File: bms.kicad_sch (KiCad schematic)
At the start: 15 parts, among them Q2 TK11S10N1L,LQ, U1 L99BM114-TR

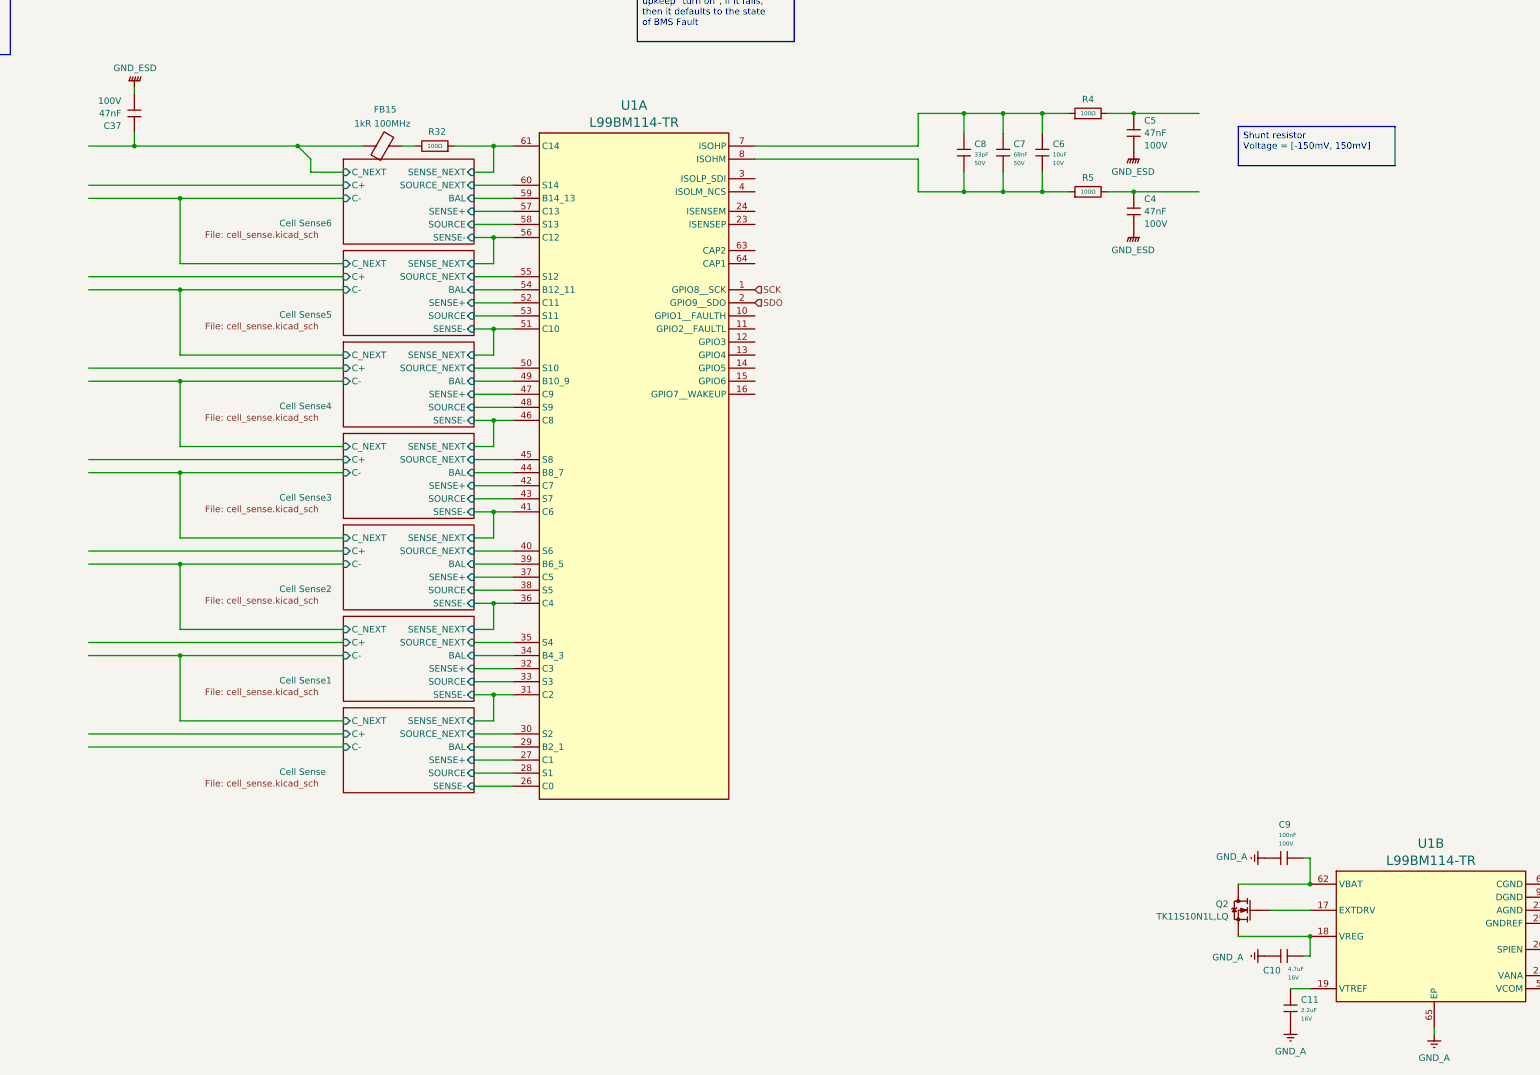
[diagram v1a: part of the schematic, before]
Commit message: updated to use generics for passives
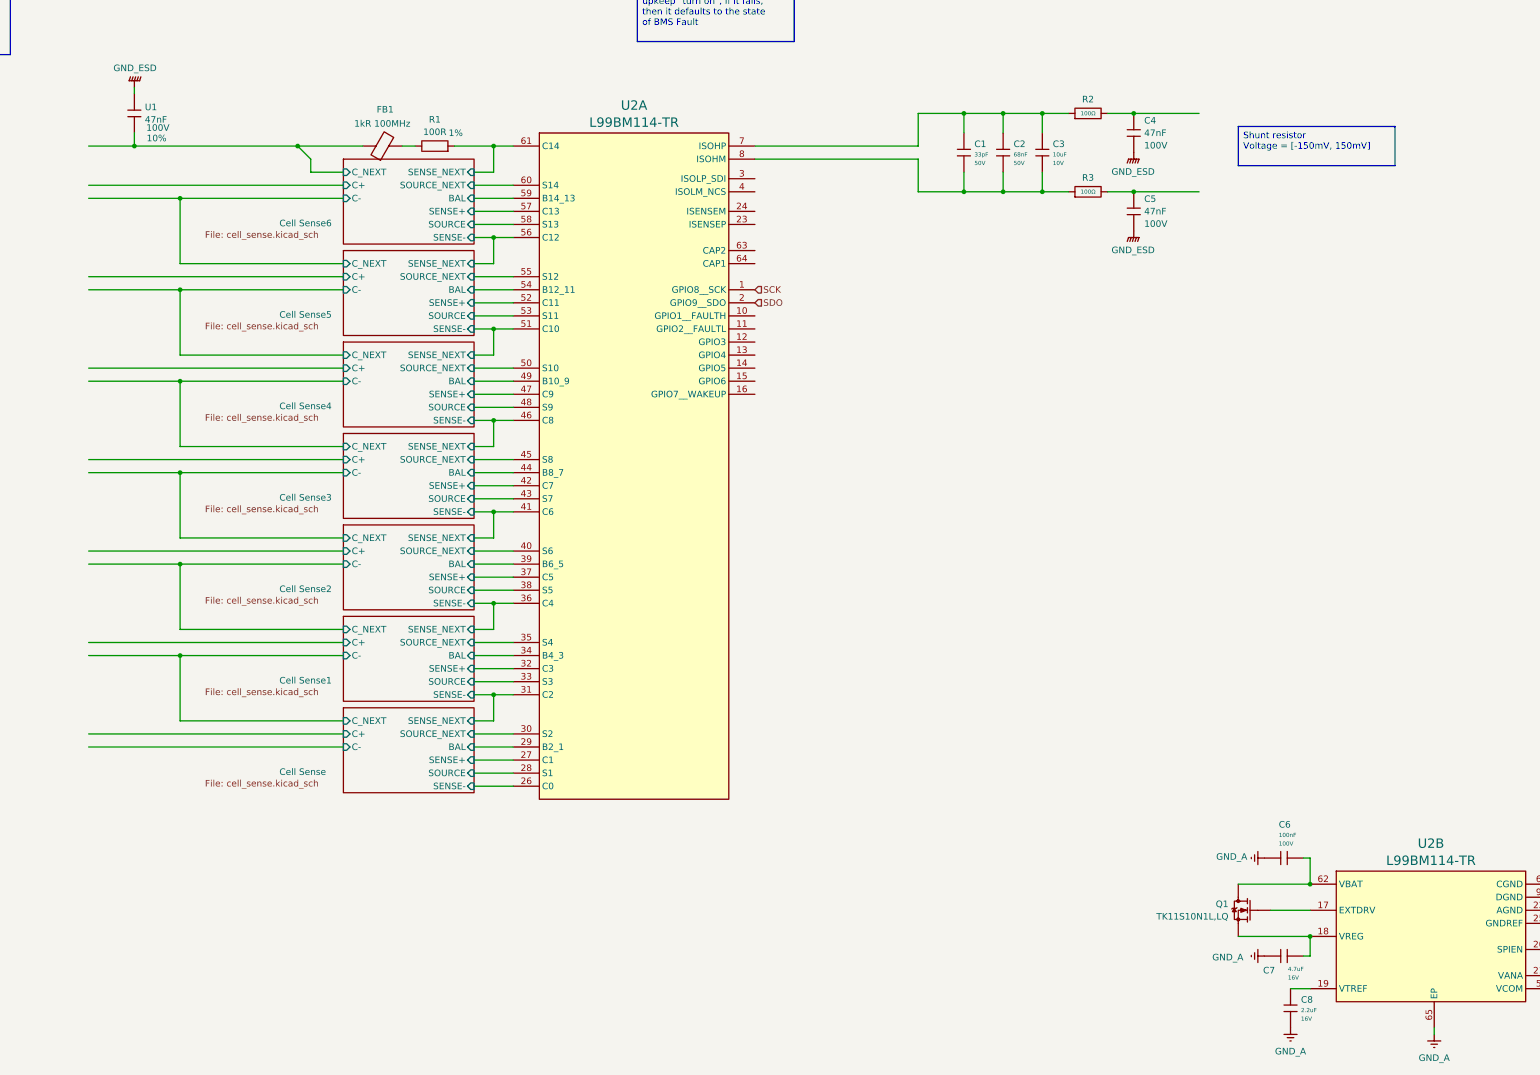
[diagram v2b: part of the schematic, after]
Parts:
- removed C37: 47nF, symbol ct_lib:CC0603KRX7R0BB473
- removed R32: 100Ω, PCM_JLCPCB:R_0402, symbol PCM_JLCPCB-Resistors:0402,100Ω
- added R1: 100R, symbol ct_lib:R
- added U1: 47nF, symbol ct_lib:C
- renumbered C8 to C1, C7 to C2, C6 to C3, C5 to C4, C4 to C5, C9 to C6, C10 to C7, C11 to C8, FB15 to FB1, Q2 to Q1, R4 to R2, R5 to R3, U1 to U2
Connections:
- net Cell Sense6/SENSE_NEXT: now also R1.2
- net GND_ESD: now also U1.1
- net at FB1.1: now also U1.2
- net at FB1.2: now also R1.1

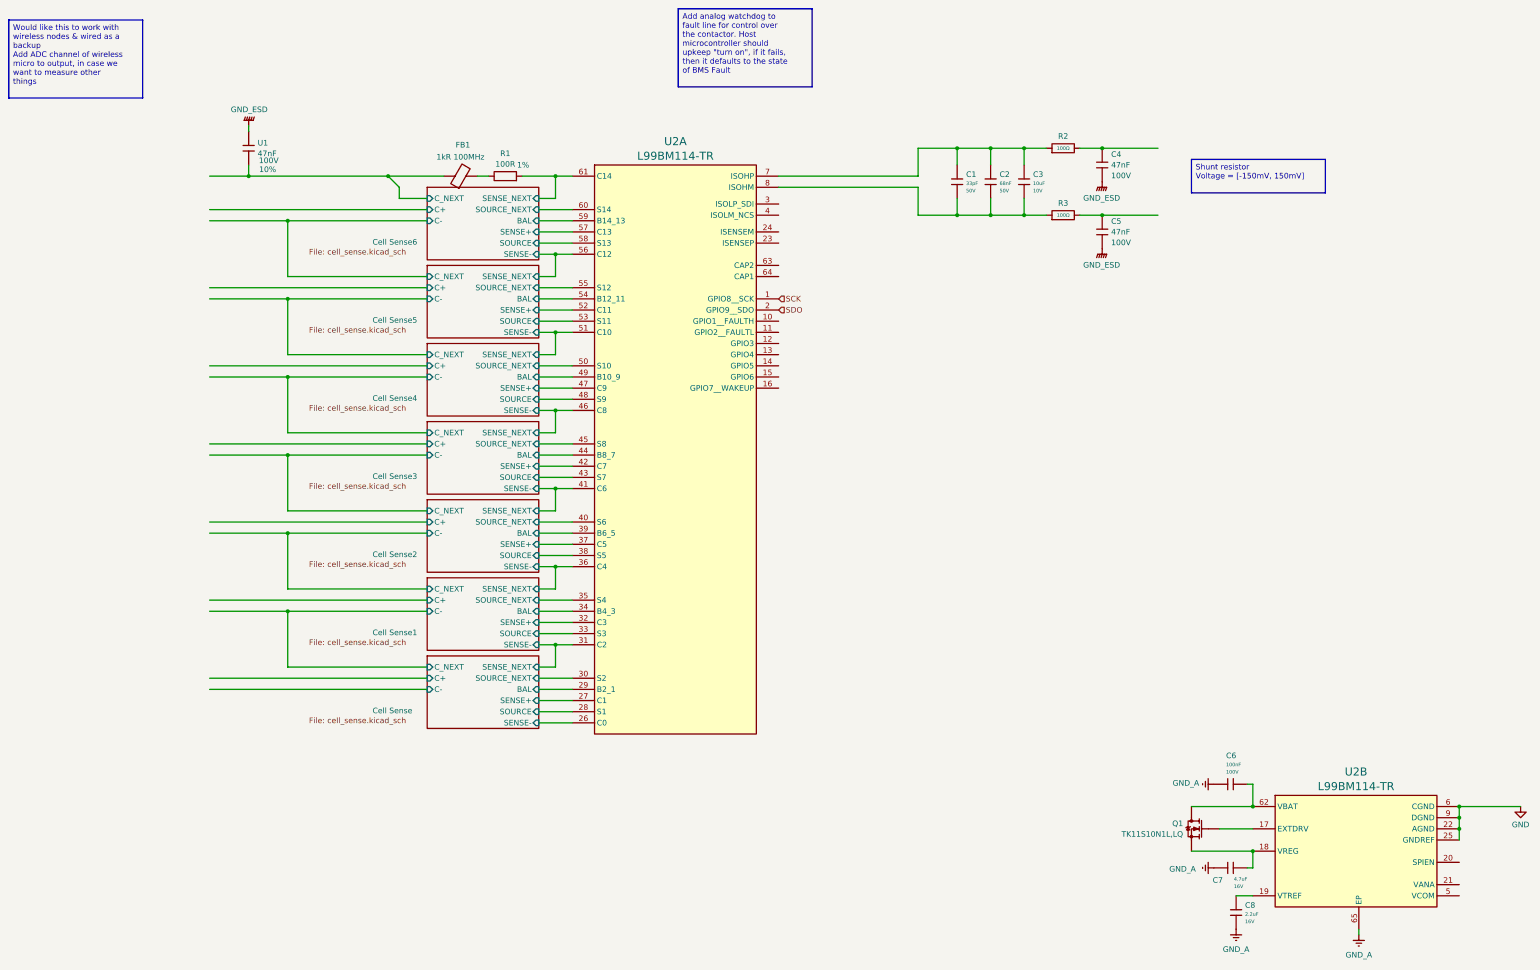
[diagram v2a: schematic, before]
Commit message: added BQ chip
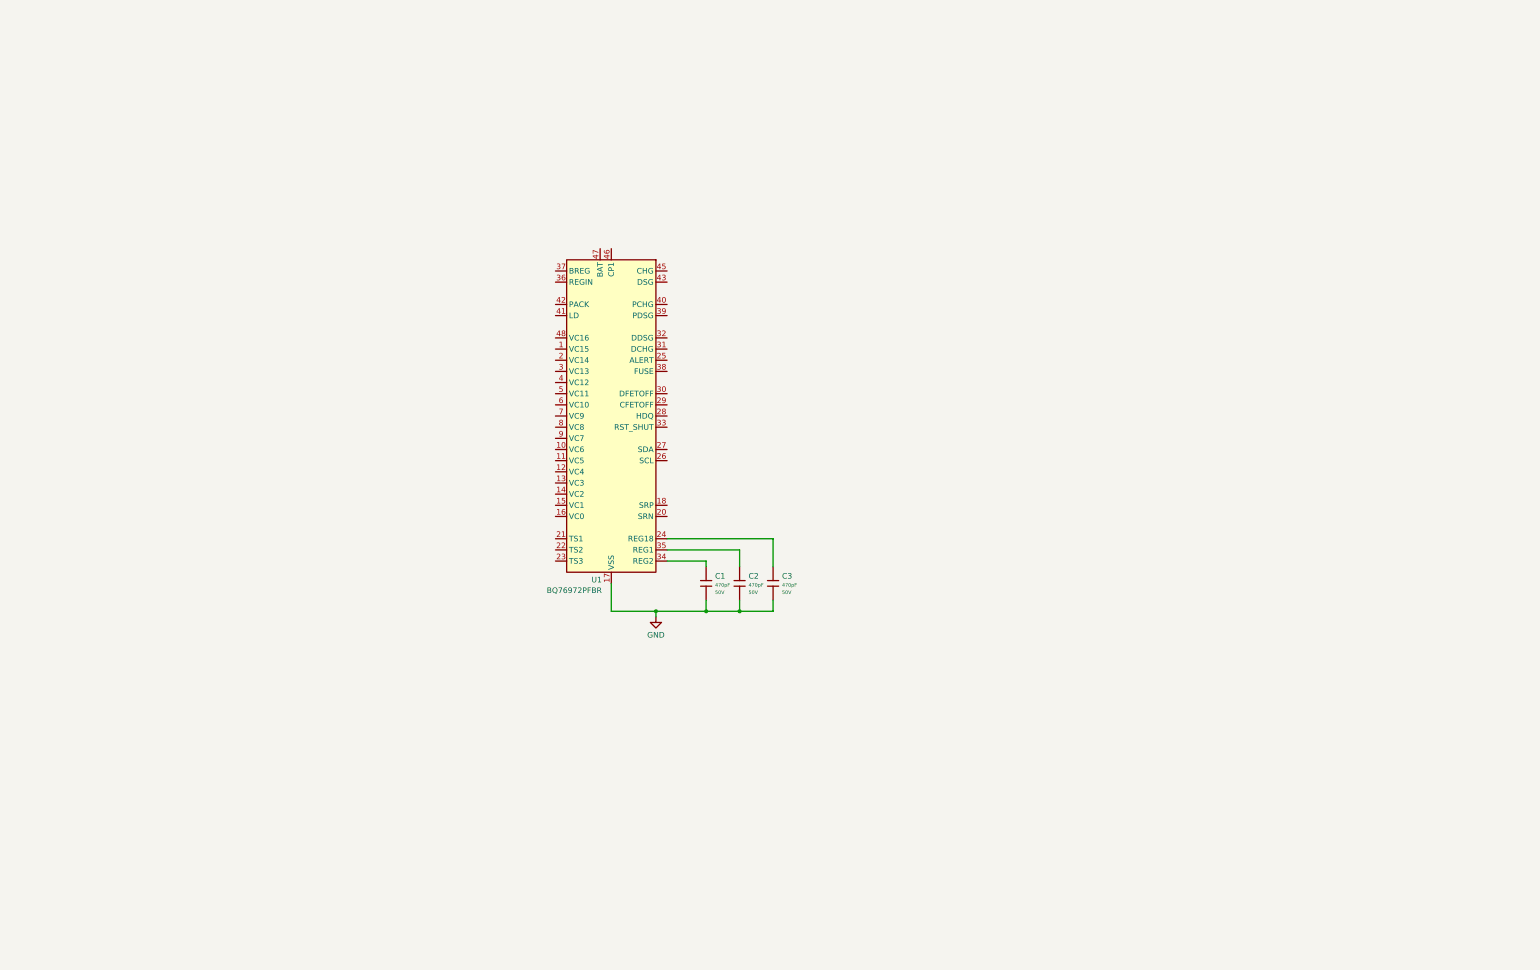
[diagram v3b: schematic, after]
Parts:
- removed C1: 33pF, PCM_JLCPCB:C_0402, symbol PCM_JLCPCB-Capacitors:0402,33pF
- removed C2: 68nF, PCM_JLCPCB:C_0603, symbol PCM_JLCPCB-Capacitors:0603,68nF
- removed C3: 10uF, PCM_JLCPCB:C_0603, symbol PCM_JLCPCB-Capacitors:0603,10uF
- removed C4, C5: 47nF, symbol ct_lib:CC0603KRX7R0BB473
- removed C6: 100nF, PCM_JLCPCB:C_0805, symbol PCM_JLCPCB-Capacitors:0805,100nF
- removed C7: 4.7uF, PCM_JLCPCB:C_0603, symbol PCM_JLCPCB-Capacitors:0603,4.7uF
- removed C8: 2.2uF, PCM_JLCPCB:C_0603, symbol PCM_JLCPCB-Capacitors:0603,2.2uF
- removed FB1: 1kR 100MHz, symbol ct_lib:MPZ2012S102ATD25
- removed Q1: TK11S10N1L,LQ, symbol ct_lib:TK11S10N1L,LQ
- removed R1: 100R, symbol ct_lib:R
- removed R2, R3: 100Ω, PCM_JLCPCB:R_0402, symbol PCM_JLCPCB-Resistors:0402,100Ω
- removed U1: 47nF, symbol ct_lib:C
- removed U2: L99BM114-TR, symbol ct_lib:L99BM114-TR
- added C1, C2, C3: 470pF, PCM_JLCPCB:C_0402, symbol PCM_JLCPCB-Capacitors:0402,470pF
- added U1: BQ76972PFBR, symbol ct_lib:BQ76972PFBR
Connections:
- net GND: now also C1.2, C2.2, C3.2, U1.17 (VSS)
- new net: C1.1, U1.34 (REG2)
- new net: C3.1, U1.24 (REG18)
- new net: C2.1, U1.35 (REG1)
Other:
- removed sheet Cell Sense
- removed sheet Cell Sense1
- removed sheet Cell Sense2
- removed sheet Cell Sense3
- removed sheet Cell Sense4
- removed sheet Cell Sense5
- removed sheet Cell Sense6
